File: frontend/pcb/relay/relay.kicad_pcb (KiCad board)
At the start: 2 copper layers, 17 parts, among them J1 Conn_01x02, J2 Conn_01x02, J3 CONN_01X02, J4 Conn_01x02, K1 G6B-1114C-US5DC, Q3 BSS138, U2 DSN-MINI-360

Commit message: Finish relay board.
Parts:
- removed H3, H4: MountingHole, MountingHole:MountingHole_3.2mm_M3
- removed J4: Conn_01x02, Connector_JST:JST_XH_B2B-XH-A_1x02_P2.50mm_Vertical
- J1: value Conn_01x02 -> Conn_01x03; footprint Connector_JST:JST_XH_B2B-XH-A_1x02_P2.50mm_Vertical -> Connector_PinSocket_2.54mm:PinSocket_1x03_P2.54mm_Vertical; moved to B.Cu
- moved H2 71.8 mm to (97.1, 105.0)
- moved H1 50.1 mm to (55.0, 105.0)
- moved J2 45.9 mm to (96.5, 92.7), turned to 90 degrees
- moved R3 38.0 mm to (62.0, 90.1), turned to -90 degrees
- moved R4 35.4 mm to (58.6, 87.4), turned to 180 degrees
- moved J3 32.7 mm to (62.5, 104.6)
- moved C5 30.8 mm to (81.8, 85.1), turned to -90 degrees
- moved K1 29.2 mm to (71.1, 84.3)
- moved J1 29.1 mm to (55.0, 85.0), turned to 180 degrees
- moved Q3 29.0 mm to (64.5, 90.4)
- moved D2 27.5 mm to (68.1, 86.5), turned to 90 degrees
- moved D1 25.7 mm to (77.7, 106.2)
- moved U2 21.7 mm to (87.4, 99.6), turned to -90 degrees
- moved TP1 16.9 mm to (88.9, 85.3)
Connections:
- J1 pad 1: +12V -> GND
- J1 pad 2: GND -> Relay
- J3 pad 1: Net-(J3-Pin_1) -> GND
- J3 pad 2: GND -> Net-(J3-Pin_2)
- K1 pad 4: Net-(J3-Pin_1) -> Net-(J3-Pin_2)
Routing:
- net GND: track 0.00 -> 114.3 mm, vias 0 -> 2
- net +5V: track 0.00 -> 57.7 mm
- net +12V: track 0.00 -> 29.1 mm
- net Net-(D2-A): track 0.00 -> 9.90 mm
- net Net-(J3-Pin_2): track 0.00 -> 7.15 mm
- net Net-(Q3-G): track 0.00 -> 4.97 mm
- net Net-(D1-A): track 0.00 -> 3.50 mm
- net Relay: track 0.00 -> 2.93 mm
- added copper zone on B.Cu, net GND
- added copper zone on F.Cu, net GND
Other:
- board outline added: 49.9 x 26.3 mm
- board text added: "12V"
- board text added: "Lock"

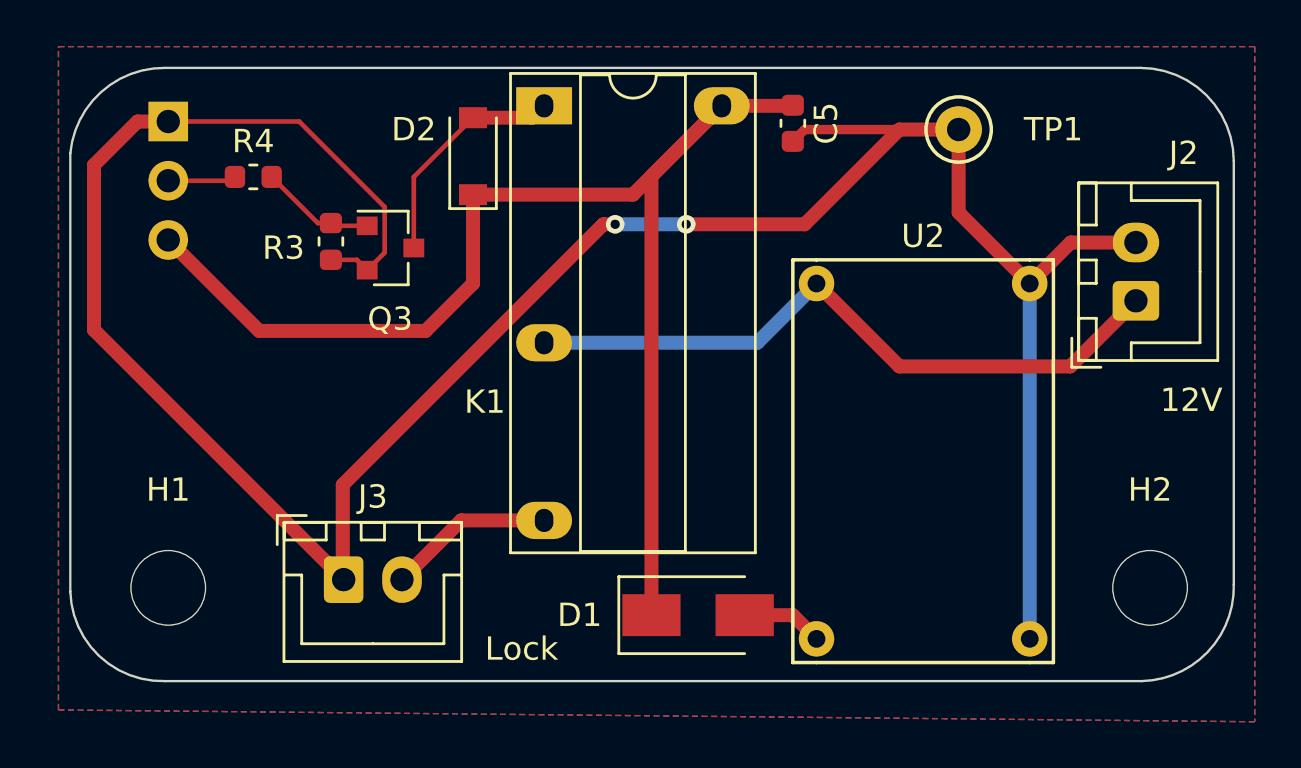
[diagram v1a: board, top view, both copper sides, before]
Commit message: Add filter resistor.
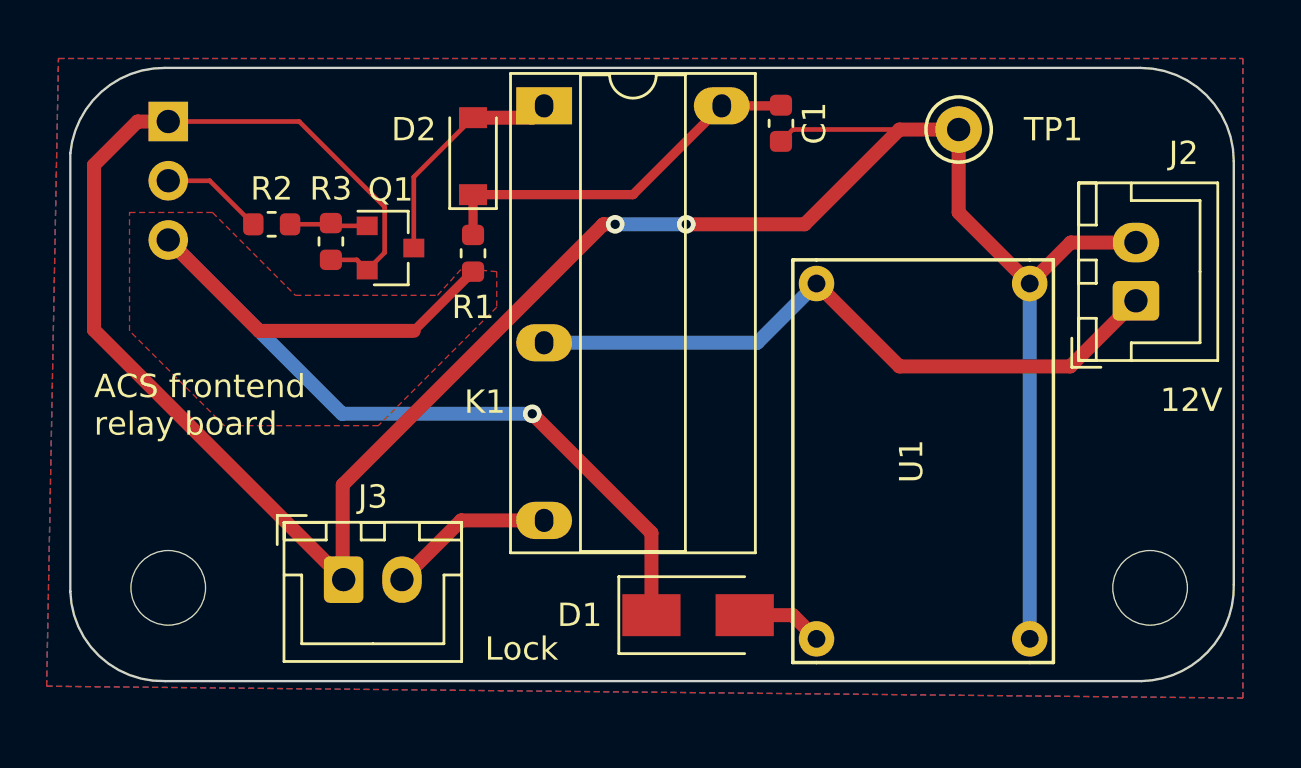
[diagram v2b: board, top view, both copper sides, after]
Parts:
- removed C5: 10u, Capacitor_SMD:C_0603_1608Metric
- removed Q3: BSS138, Package_TO_SOT_SMD:SOT-23
- removed R4: 1K, Resistor_SMD:R_0603_1608Metric
- removed U2: DSN-MINI-360, modules:DSN-MINI-360
- added C1: 10u, Capacitor_SMD:C_0603_1608Metric, F.Cu at (81.3, 85.1)
- added Q1: BSS138, Package_TO_SOT_SMD:SOT-23, F.Cu at (64.5, 90.4)
- added R1: 4R7, Resistor_SMD:R_0603_1608Metric, F.Cu at (68.1, 90.7)
- added R2: 1K, Resistor_SMD:R_0603_1608Metric, F.Cu at (59.4, 89.4)
- added U1: DSN-MINI-360, modules:DSN-MINI-360, F.Cu at (87.4, 99.6)
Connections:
- D2 pad 1: +5V -> Net-(D2-K)
- K1 pad 2: +5V -> Net-(D2-K)
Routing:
- net Net-(D2-K): track 0.00 -> 16.5 mm
- net +5V: track 57.7 -> 45.2 mm, vias 0 -> 1
- net Net-(Q1-G): track 4.97 -> 3.38 mm
- net Relay: track 2.93 -> 4.42 mm
- net GND: track 114.3 -> 114.8 mm
- added copper zone on F.Cu, net +5V
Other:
- board text added: "ACS frontend relay board"
- board text added: "https://github.com/bullestock/acsv2"

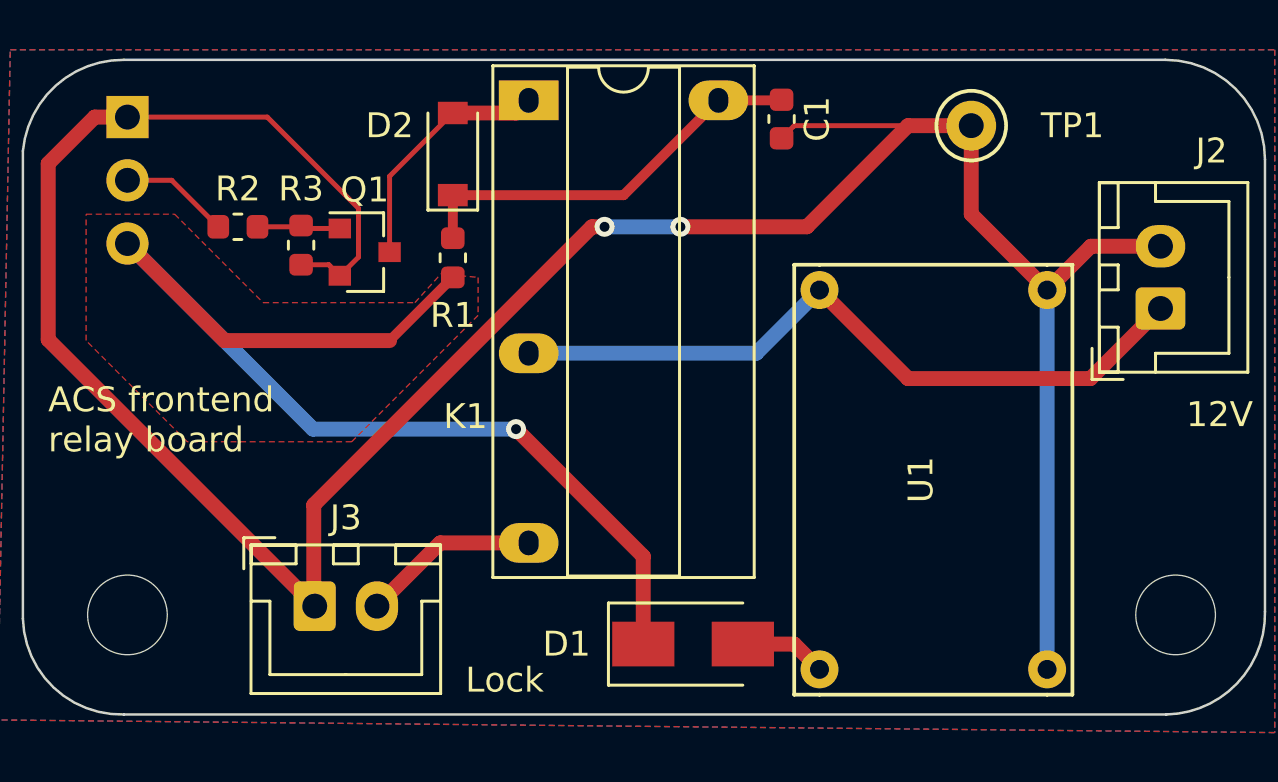
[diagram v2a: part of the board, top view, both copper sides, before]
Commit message: Increase capacitor value.
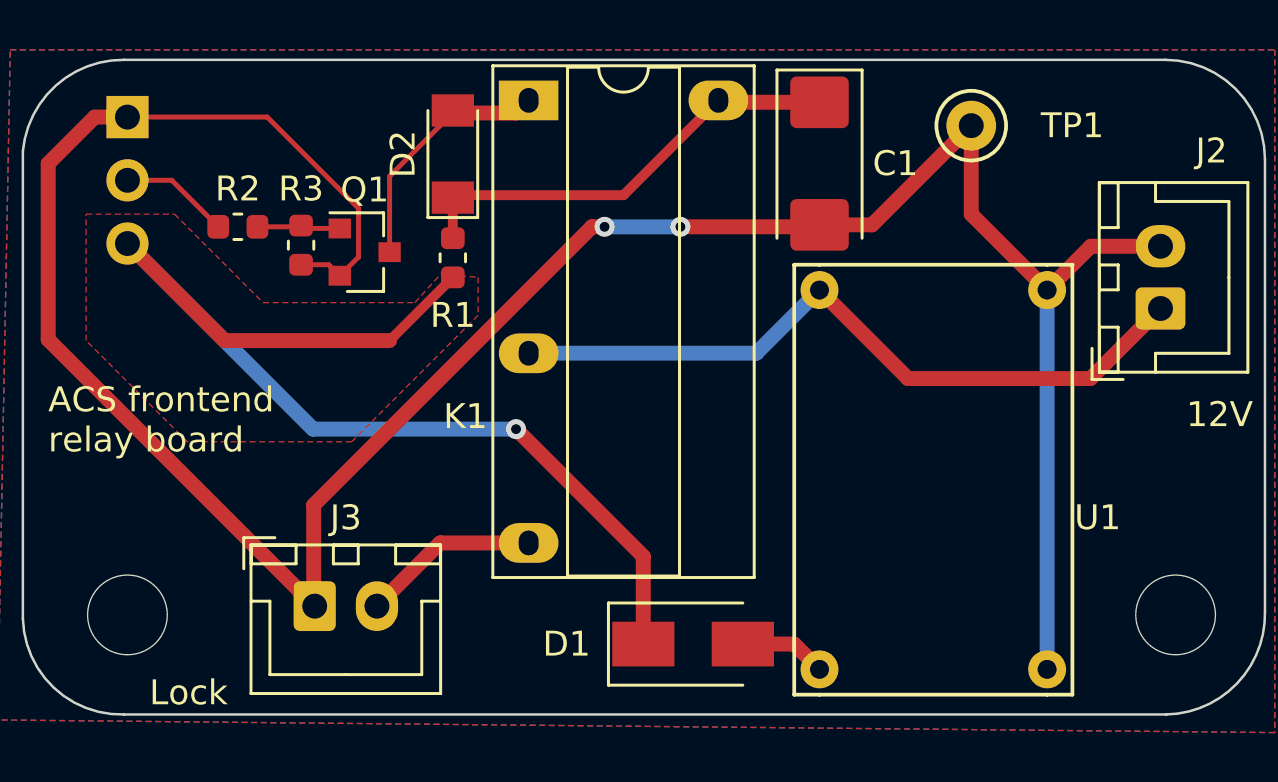
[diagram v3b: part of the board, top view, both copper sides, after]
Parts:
- C1: value 10u -> 220u; footprint Capacitor_SMD:C_0603_1608Metric -> Capacitor_Tantalum_SMD:CP_EIA-6032-28_Kemet-C
- D2: footprint Diode_SMD:D_SOD-123 -> Diode_SMD:D_MiniMELF
- moved C1 2.35 mm to (82.8, 86.9)
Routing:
- net GND: track 114.8 -> 106.9 mm
- net Net-(D2-K): track 16.5 -> 18.1 mm

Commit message: Final adjustments, order.
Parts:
- moved TP1 29.2 mm to (69.7, 107.4)
- moved J2 11.5 mm to (87.5, 85.6), turned to 0 degrees
- moved C1 0.38 mm to (82.4, 86.8)
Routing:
- net +12V: track 29.1 -> 22.0 mm
- net GND: track 106.9 -> 108.8 mm
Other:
- outline, holes or cut-outs redrawn
